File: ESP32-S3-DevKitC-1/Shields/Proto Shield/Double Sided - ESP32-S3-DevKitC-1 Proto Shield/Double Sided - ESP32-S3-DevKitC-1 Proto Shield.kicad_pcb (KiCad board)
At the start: 2 copper layers, 43.2 x 69.1 mm, 0 parts

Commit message: Finished front side of ESP32-S3 proto shield in kicad
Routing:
- net (no net): track 580.9 -> 1281.5 mm, vias 0 -> 818
- net -1: vias 402 -> 0
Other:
- board size 43.2 x 69.1 mm -> 107.7 x 83.8 mm
- board text added: "H17"
- board text added: "H18"
- board text added: "H19"
- board text added: "M/N: JDS2.COM/AAB/001"
- board text added: "SW_BOOT"
- board text added: "SW_RESET"
- board text added: "VER: 01.00.00"
- board text added: "locked"

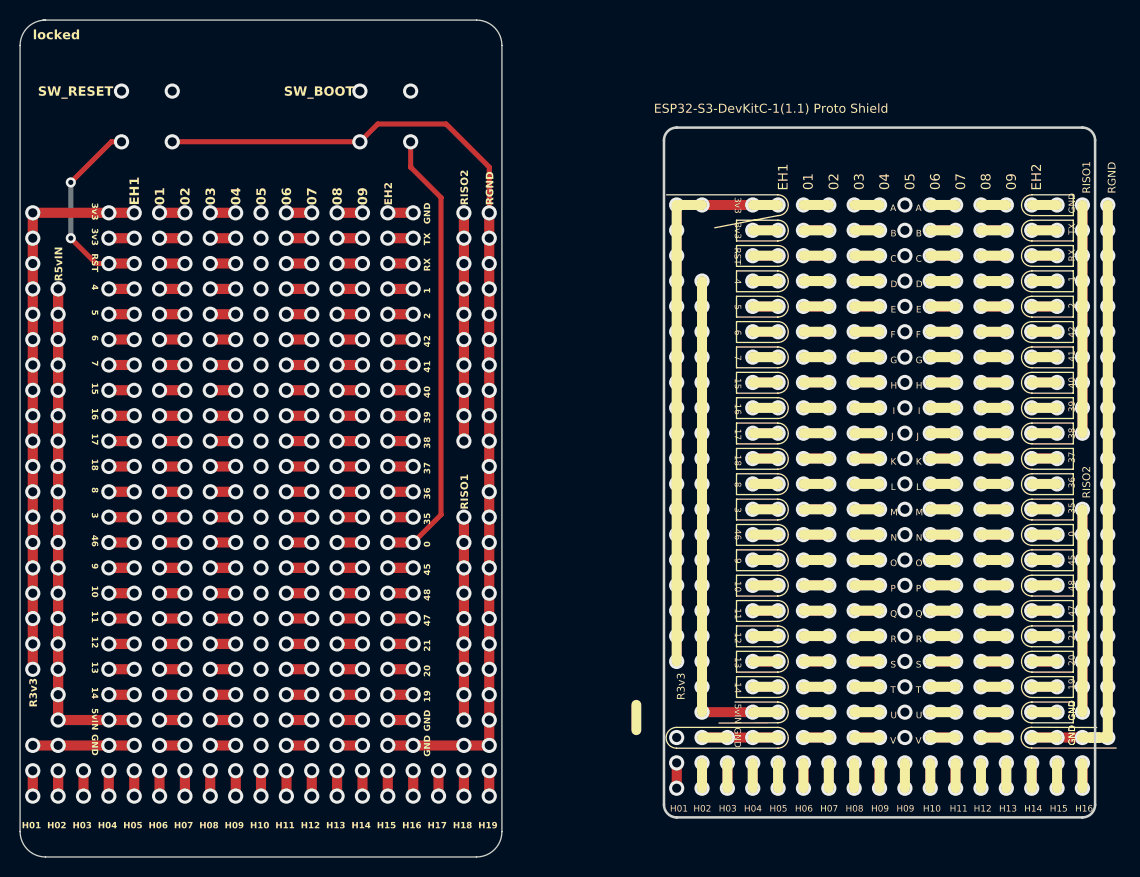
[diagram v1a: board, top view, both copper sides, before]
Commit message: version 01.00.00 as ordered through JLCPCB
- Rails moved back
- Two switch/buttons added
- Started using KICad
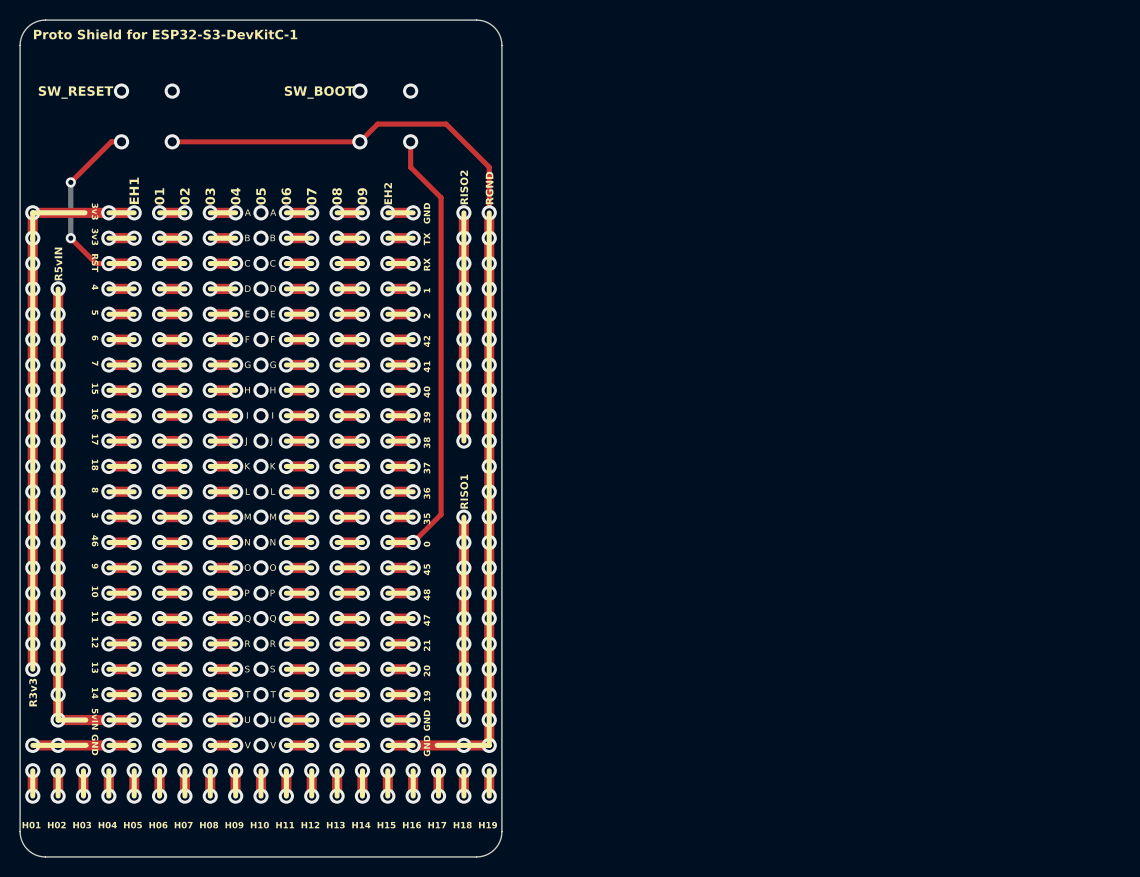
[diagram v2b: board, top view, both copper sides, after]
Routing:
- net (no net): track 1281.5 -> 695.5 mm, vias 818 -> 415
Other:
- board size 107.7 x 83.8 mm -> 48.3 x 83.8 mm
- rule pad_to_mask_clearance: 0 -> 0.0254
- board text added: "Proto Shield for ESP32-S3-DevKitC-1"
- board text removed: "ESP32-S3-DevKitC-1(1.1) Proto Shield"
- board text removed: "M/N: JDS2.COM/AAB/001 - VER: 00.00.03"
- board text removed: "locked"
